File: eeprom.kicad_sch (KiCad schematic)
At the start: 9 parts, among them J19 WP Jumper, U9 AT24C64D

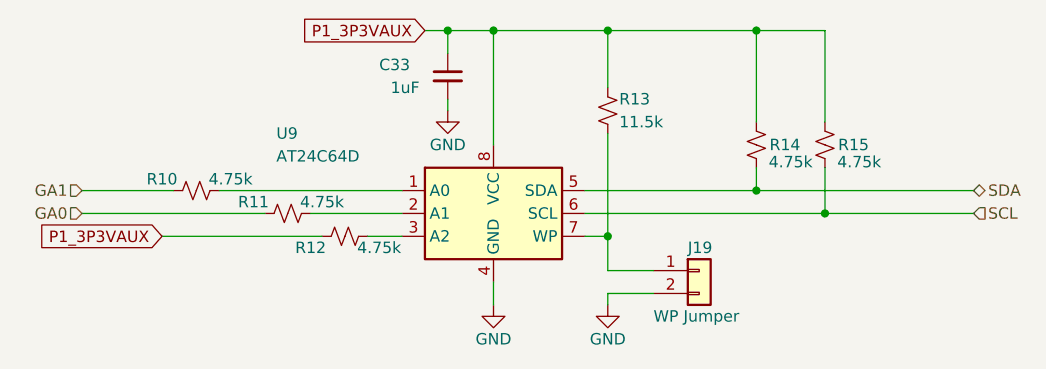
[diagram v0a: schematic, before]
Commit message: Changed layout, added 12V and Heart LEDs
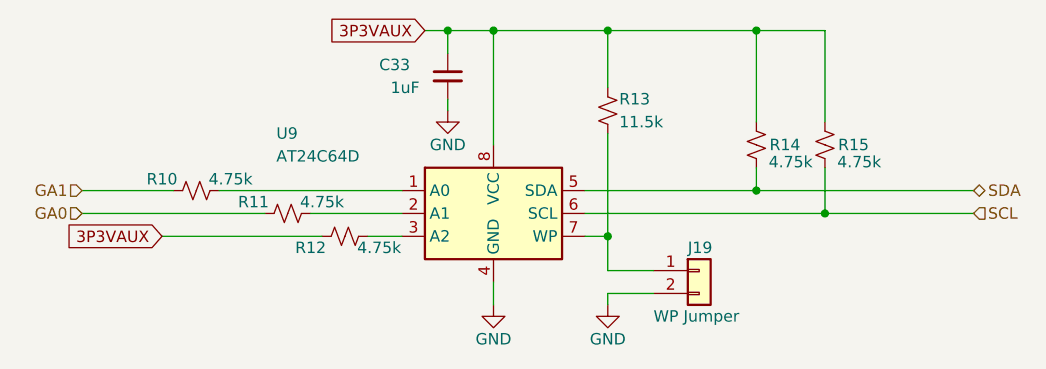
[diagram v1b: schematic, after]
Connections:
- net P1_3P3VAUX renamed 3P3VAUX
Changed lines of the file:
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@@
 		)
 	)
-	(global_label "P1_3P3VAUX"
+	(global_label "3P3VAUX"
 		(shape input)
 		(at 130.81 81.28 180)
@@
 		)
 		(property "Intersheetrefs" "${INTERSHEET_REFS}"
-			(at 116.0509 81.28 0)
+			(at 119.4186 81.28 0)
 			(effects
 				(font
@@
 		)
 	)
-	(global_label "P1_3P3VAUX"
+	(global_label "3P3VAUX"
 		(shape input)
 		(at 101.6 104.14 180)
@@
 		)
 		(property "Intersheetrefs" "${INTERSHEET_REFS}"
-			(at 86.7615 104.14 0)
+			(at 90.2086 104.14 0)
 			(effects
 				(font
